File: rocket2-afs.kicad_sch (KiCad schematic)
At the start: 62 parts, among them J1 ARMING_PLUG, J2 POWER, J3 E-MATCH_DROGUE, J4 SWD, J5 E-MATCH_RECOVERY, Q1 Q_NMOS_GSD, Q2 Q_NMOS_GSD, Q3 Q_NMOS_GSD, Q4 Q_NMOS_GSD, U2 LD1086DT33TR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

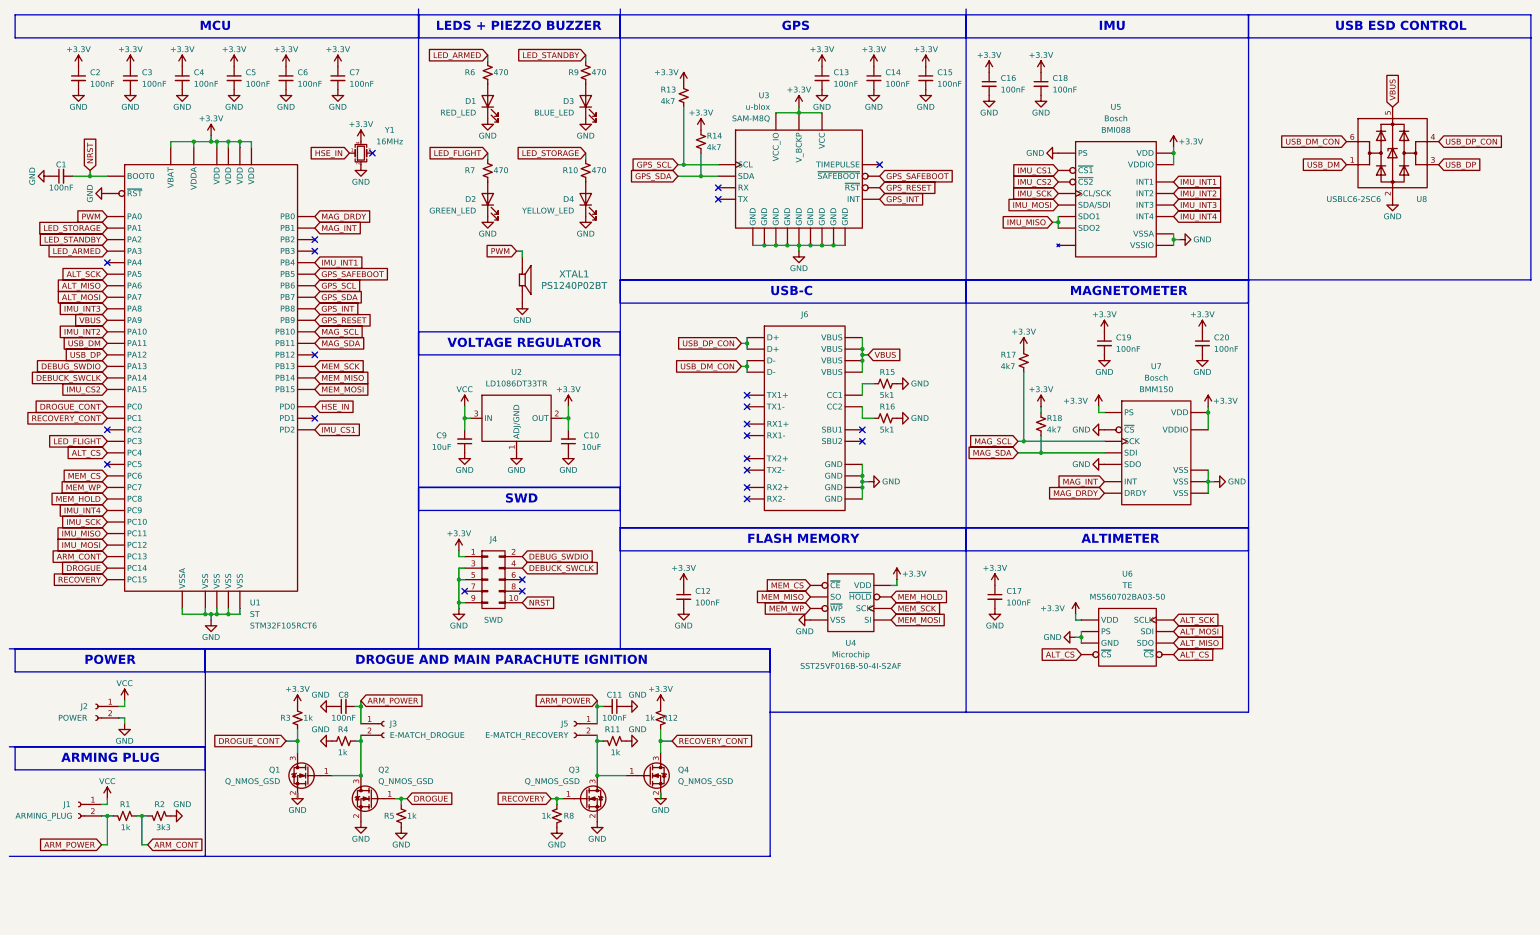
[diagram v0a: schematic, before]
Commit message: Fixed HSE pinout. Updated Crystal circuit.
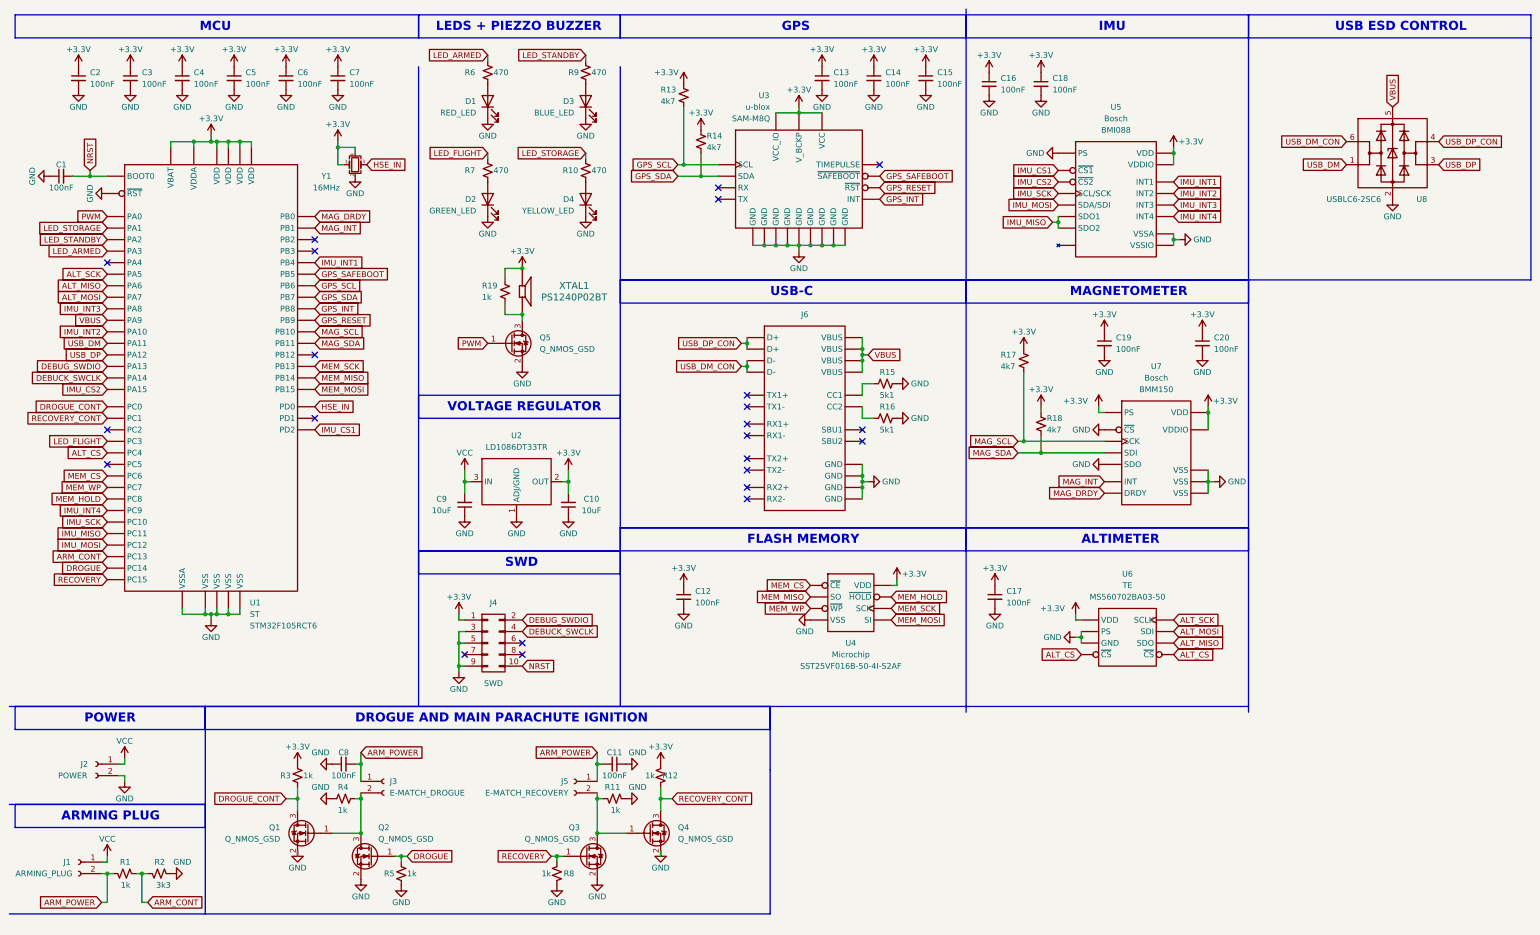
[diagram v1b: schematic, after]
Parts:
- added Q5: Q_NMOS_GSD, Package_TO_SOT_SMD:TSOT-23, symbol Device:Q_NMOS_GSD
- added R19: 1k, Resistor_SMD:R_0603_1608Metric, symbol Device:R_Small_US
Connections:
- net +3.3V: now also XTAL1.1, Y1.1, R19.1
- net GND: now also Q5.2 (S); no longer XTAL1.2
- net HSE_IN: now also Y1.3; no longer Y1.1
- net PWM: now also Q5.1 (G); no longer XTAL1.1
- new net: Q5.3 (D), R19.2, XTAL1.2
- no-connect marks 24 -> 23
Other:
- moved on the sheet: C10, C11, C8, C9, J1, J2, J3, J4, J5, Q1, Q2, Q3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

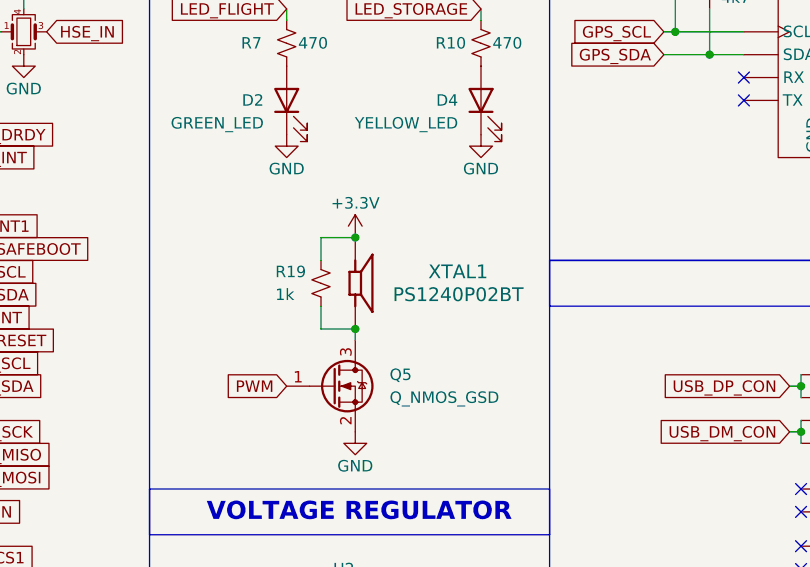
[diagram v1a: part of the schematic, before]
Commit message: Adjusted Symbol Libraries for USB-C and Piezo Buzzer
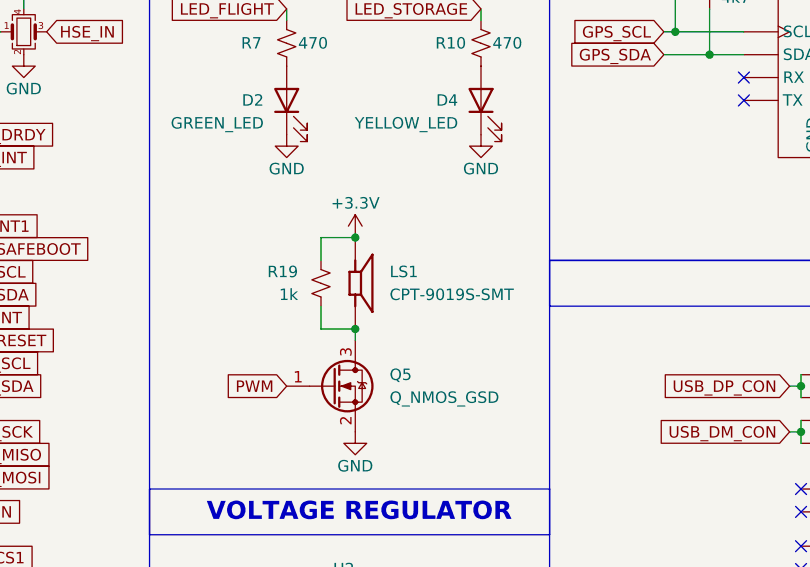
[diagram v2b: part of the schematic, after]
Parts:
- removed XTAL1: PS1240P02BT, CUI_CPT-9019S-SMT, symbol Piezo Buzzer:CPT-9019S-SMT
- added LS1: CPT-9019S-SMT, UCIRP-KiCAD-Lib:CUI_CPT-9019S-SMT, symbol UCIRP-KiCAD-Lib:CPT-9019S-SMT
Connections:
- net +3.3V: now also LS1.1
- net at Q5.3 (D), R19.2: now also LS1.2
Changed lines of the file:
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@@
 (kicad_sch (version 20230121) (generator eeschema)
   (paper "A3")
-  (junction (at 124.46 68.58) (diameter 0) (color 0 0 0 0)
-  )
   (junction (at 185.42 34.29) (diameter 0) (color 0 0 0 0)
   )
@@
   (junction (at 57.15 144.78) (diameter 0) (color 0 0 0 0)
   )
+  (junction (at 124.46 78.74) (diameter 0) (color 0 0 0 0)
+  )
   (junction (at 199.39 115.57) (diameter 0) (color 0 0 0 0)
   )
+  (junction (at 124.46 68.58) (diameter 0) (color 0 0 0 0)
+  )
   (junction (at 55.88 144.78) (diameter 0) (color 0 0 0 0)
   )
@@
   (junction (at 97.79 198.12) (diameter 0) (color 0 0 0 0)
   )
-  (junction (at 124.46 78.74) (diameter 0) (color 0 0 0 0)
-  )
   (junction (at 160.02 45.72) (diameter 0) (color 0 0 0 0)
   )
@@
     )
   )
-  (symbol (lib_id "Piezo Buzzer:CPT-9019S-SMT") (at 124.46 73.66 0) (unit 1)
-    (in_bom yes) (on_board yes) (dnp no)
-    (property "Reference" "XTAL1" (at 135.89 72.39 0)
-      (effects (font (size 1.524 1.524)))
-    )
-    (property "Value" "PS1240P02BT" (at 135.89 74.93 0)
-      (effects (font (size 1.524 1.524)))
-    )
-    (property "Footprint" "CUI_CPT-9019S-SMT" (at 124.46 73.66 0)
-      (effects (font (size 1.27 1.27)) (justify left bottom) hide)
-    )
-    (property "Datasheet" "https://www.cuidevices.com/product/resource/cpt-9019s-smt-tr.pdf" (at 124.46 73.66 0)
-      (effects (font (size 1.27 1.27)) (justify left bottom) hide)
-    )
-    (property "MANUFACTURER" "CUI INC" (at 124.46 73.66 0)
-      (effects (font (size 1.27 1.27)) (justify left bottom) hide)
-    )
-    (property "PART_REV" "1.0" (at 124.46 73.66 0)
-      (effects (font (size 1.27 1.27)) (justify left bottom) hide)
-    )
-    (property "STANDARD" "MANUFACTURER RECOMMENDATIONS" (at 124.46 73.66 0)
-      (effects (font (size 1.27 1.27)) (justify left bottom) hide)
-    )
-    (pin "1")
-    (pin "2")
-    (instances
-      (project "rocket2-afs"
-        (path "/bb02b74a-6e6c-4d52-9615-6a7971a5afcd"
-          (reference "XTAL1") (unit 1)
-        )
-      )
-      (project "AFS2.1_Betelgeuse"
-        (path "/be554a08-147d-45c0-b8f6-ea3dd923a785"
-          (reference "XTAL1") (unit 1)
-        )
-      )
-    )
-  )
   (symbol (lib_id "Device:Q_NMOS_GSD") (at 77.47 193.04 0) (mirror y) (unit 1)
     (in_bom yes) (on_board yes) (dnp no)
@@
   (symbol (lib_id "Device:R_Small_US") (at 120.65 73.66 0) (unit 1)
     (in_bom yes) (on_board yes) (dnp no)
-    (property "Reference" "R19" (at 115.57 72.39 0)
-      (effects (font (size 1.27 1.27)) (justify left))
+    (property "Reference" "R19" (at 118.11 72.39 0)
+      (effects (font (size 1.27 1.27)) (justify right))
     )
-    (property "Value" "1k" (at 115.57 74.93 0)
-      (effects (font (size 1.27 1.27)) (justify left))
+    (property "Value" "1k" (at 118.11 74.93 0)
+      (effects (font (size 1.27 1.27)) (justify right))
     )
     (property "Footprint" "Resistor_SMD:R_0603_1608Metric" (at 120.65 73.66 0)
@@
         )
       )
+    )
+  )
+  (symbol (lib_id "UCIRP-KiCAD-Lib:CPT-9019S-SMT") (at 124.46 73.66 0) (unit 1)
+    (in_bom yes) (on_board yes) (dnp no) (fields_autoplaced)
+    (property "Reference" "LS1" (at 128.27 72.39 0)
+      (effects (font (size 1.27 1.27)) (justify left))
+    )
+    (property "Value" "CPT-9019S-SMT" (at 128.27 74.93 0)
+      (effects (font (size 1.27 1.27)) (justify left))
+    )
+    (property "Footprint" "UCIRP-KiCAD-Lib:CUI_CPT-9019S-SMT" (at 127 77.47 0)
+      (effects (font (size 1.27 1.27)) (justify left bottom) hide)
+    )
+    (property "Datasheet" "" (at 124.46 73.66 0)
+      (effects (font (size 1.27 1.27)) (justify left bottom) hide)
+    )
+    (property "MANUFACTURER" "CUI INC" (at 130.81 73.66 0)
+      (effects (font (size 1.27 1.27)) (justify left bottom) hide)
+    )
+    (property "PART_REV" "1.0" (at 127 73.66 0)
+      (effects (font (size 1.27 1.27)) (justify left bottom) hide)
+    )
+    (property "STANDARD" "MANUFACTURER RECOMMENDATIONS" (at 127 69.85 0)
+      (effects (font (size 1.27 1.27)) (justify left bottom) hide)
+    )
+    (pin "1")
+    (pin "2")
+    (instances
+      (project "rocket2-afs"
+        (path "/bb02b74a-6e6c-4d52-9615-6a7971a5afcd"
+          (reference "LS1") (unit 1)
+        )
+      )

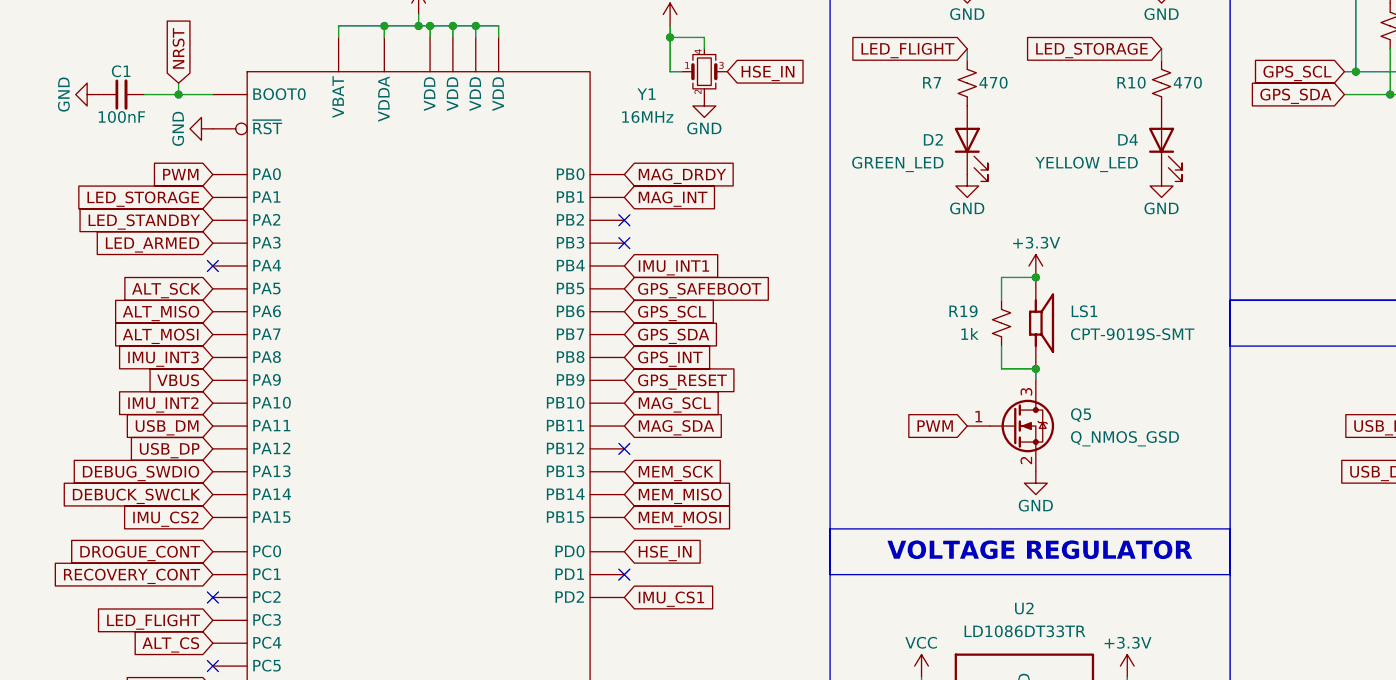
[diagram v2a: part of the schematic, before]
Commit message: New MI-9653S-SMT-TR Buzzer and Buzzer Circuit. Added power footprint.
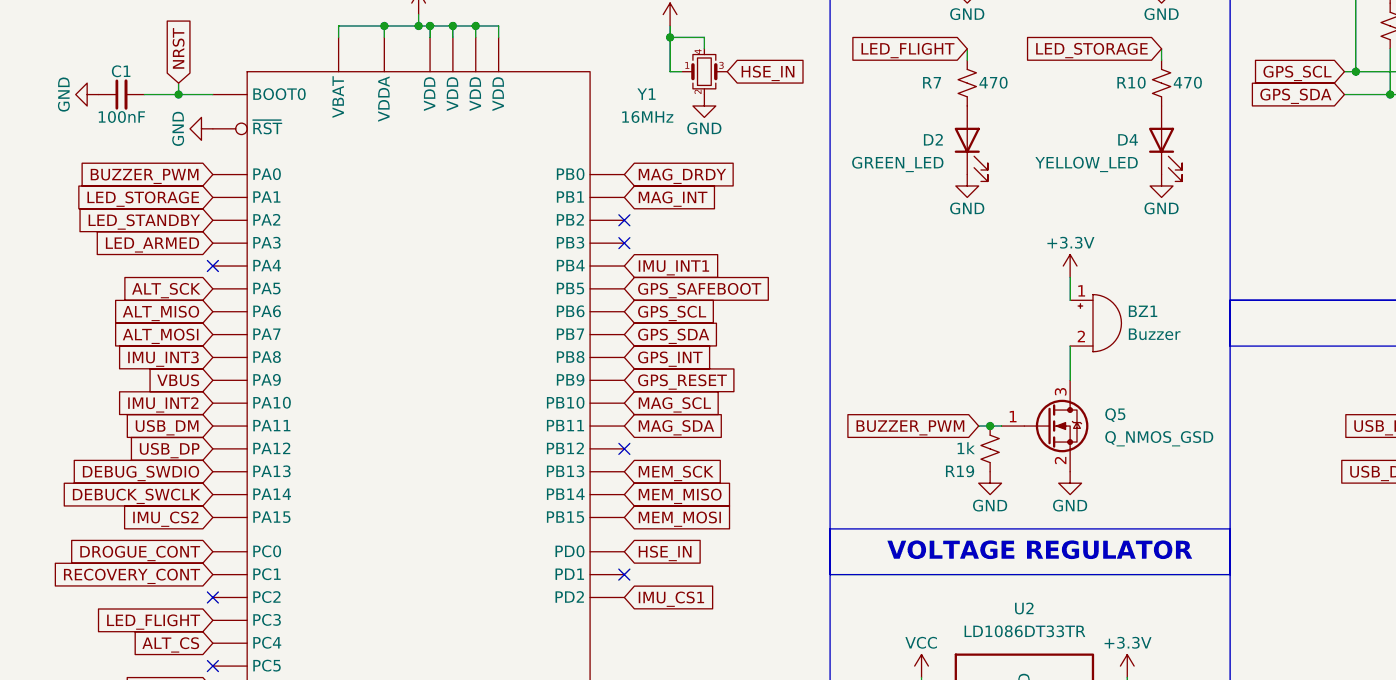
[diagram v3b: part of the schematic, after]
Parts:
- removed LS1: CPT-9019S-SMT, UCIRP-KiCAD-Lib:CUI_CPT-9019S-SMT, symbol UCIRP-KiCAD-Lib:CPT-9019S-SMT
- added BZ1: Buzzer, UCIRP-KiCAD-Lib:CUI_CMI-9653S-SMT, symbol Device:Buzzer
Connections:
- net +3.3V: now also BZ1.1 (+); no longer R19.1
- net GND: now also R19.2
- net at Q5.3 (D): now also BZ1.2 (-); no longer R19.2
- net PWM renamed BUZZER_PWM
- net BUZZER_PWM: now also R19.1
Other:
- moved on the sheet: Q5
